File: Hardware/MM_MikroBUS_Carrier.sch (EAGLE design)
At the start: 50 parts, among them J15 MICROMOD-2222-C, J2 QWIIC_RIGHT_ANGLE, J5 Vertical Qwiic Connector, J7 MIKROBUS_SMD_BLACK1, U1 MCP73831, U2 AP7361C-33FGEUDFN-8

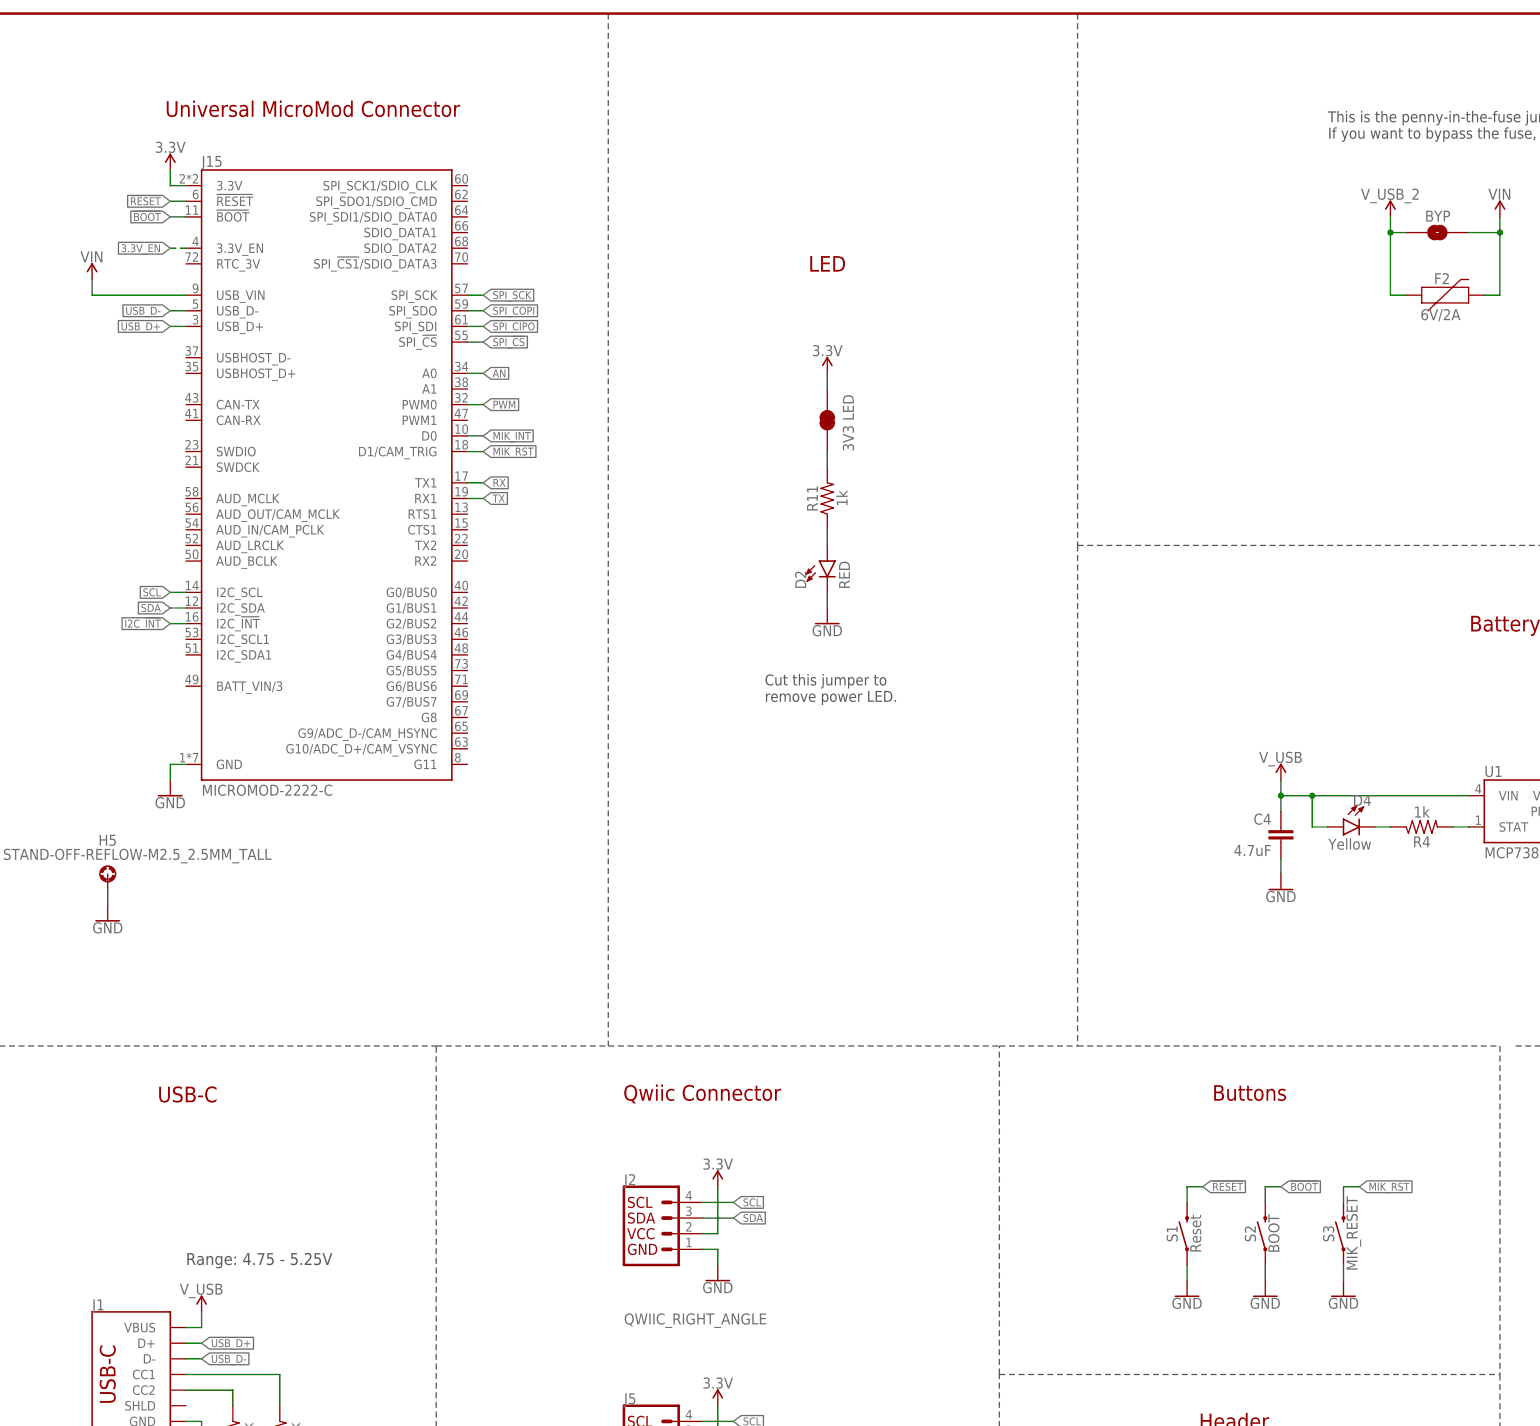
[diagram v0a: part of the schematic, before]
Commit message: MikroE updates
* Add JTAG connector
* Remove mikroE reset button
* Moved mikroBUS labels so that they can all be seen when socket is populated
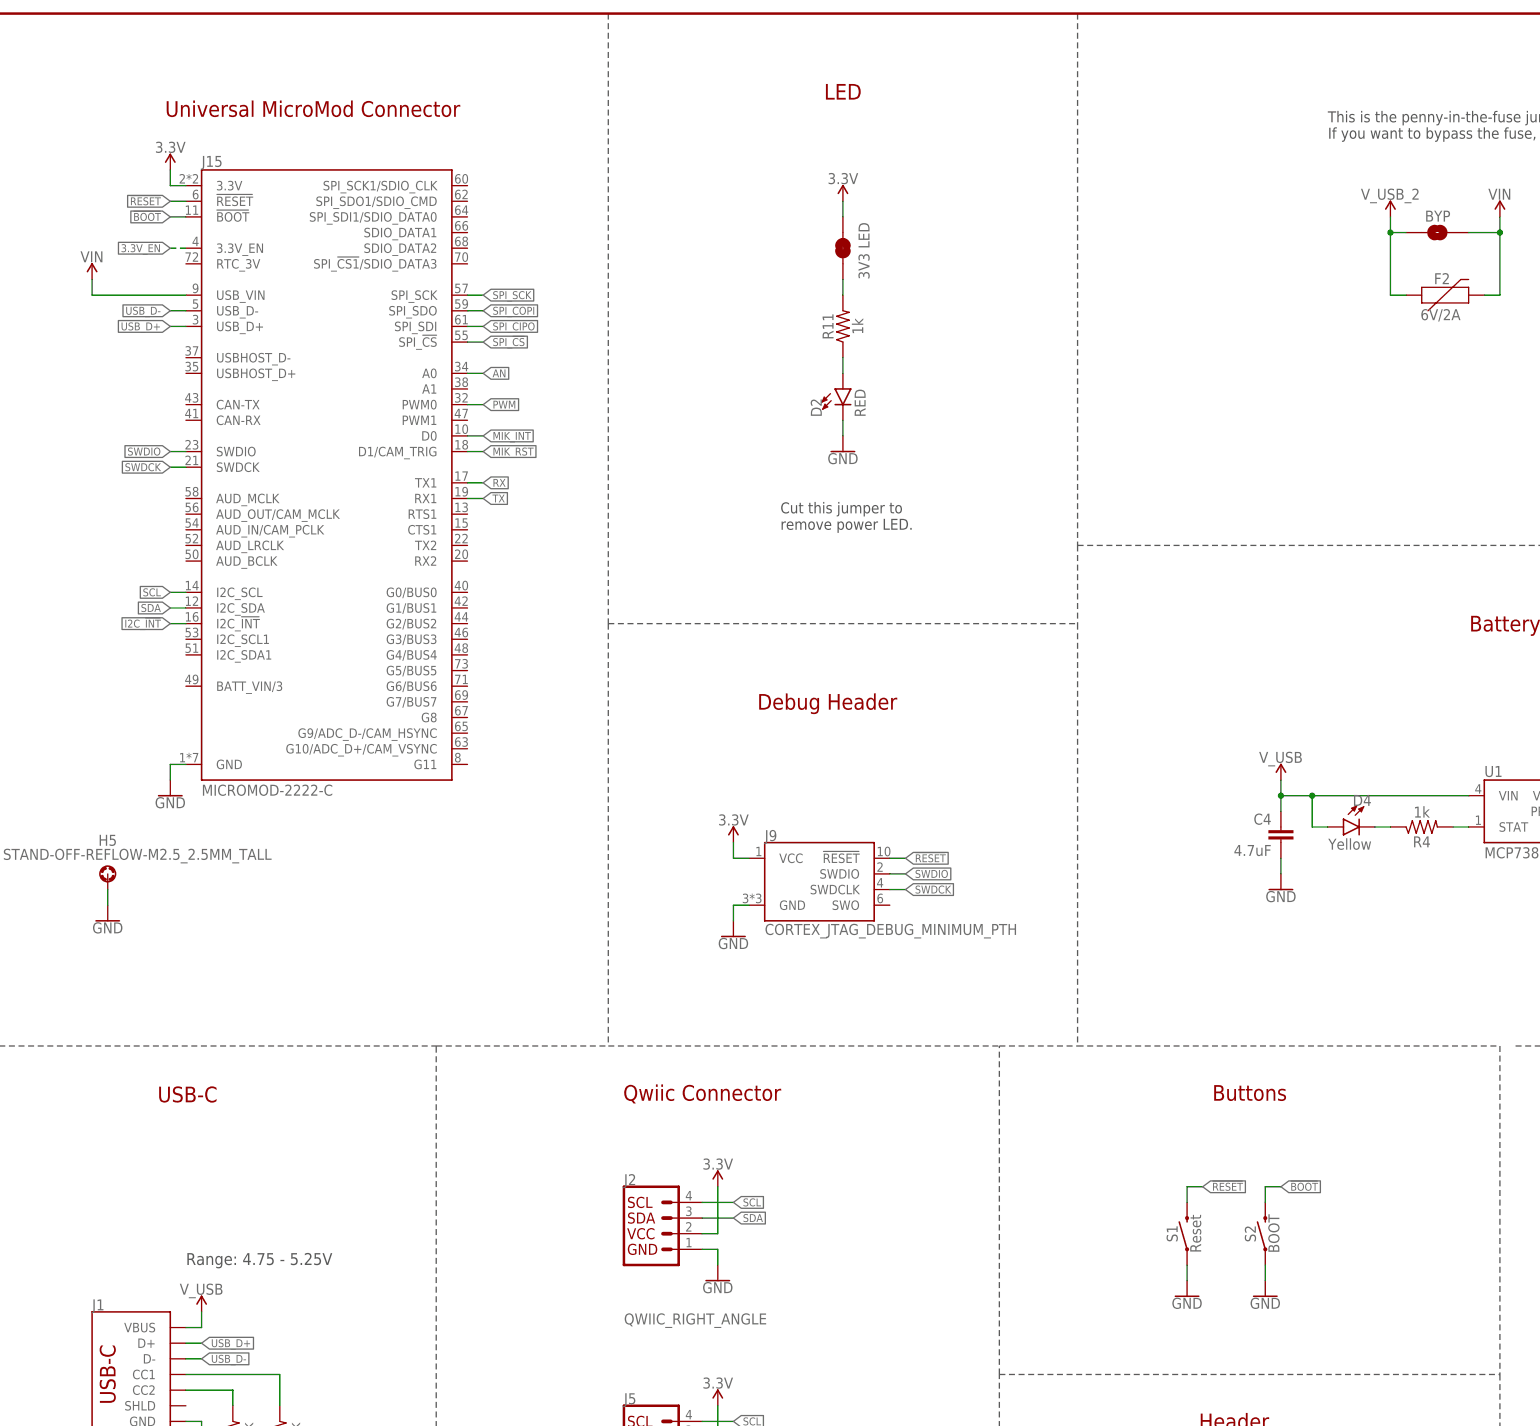
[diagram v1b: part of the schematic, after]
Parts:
- removed S3: MIK_RESET, SparkFun-Switches:MOMENTARY-SWITCH-SPST-SMD-5.2-TALL-REDUNDANT
- added J9: CORTEX_JTAG_DEBUG_MINIMUM_PTH, SparkFun-Connectors:CORTEX_JTAG_DEBUG_MINIMUM_PTH
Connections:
- new net SWDCK: J15.SWDCK, J9.SWDCLK
- new net SWDIO: J15.SWDIO, J9.SWDIO
- net !RESET!: now also J9.!RESET
- net 3.3V: now also J9.VCC
- net GND: now also J9.GND; no longer S3.1
- net MIK_RST: no longer S3.2
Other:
- note added: "Debug Header"
- moved on the sheet: D2, R11

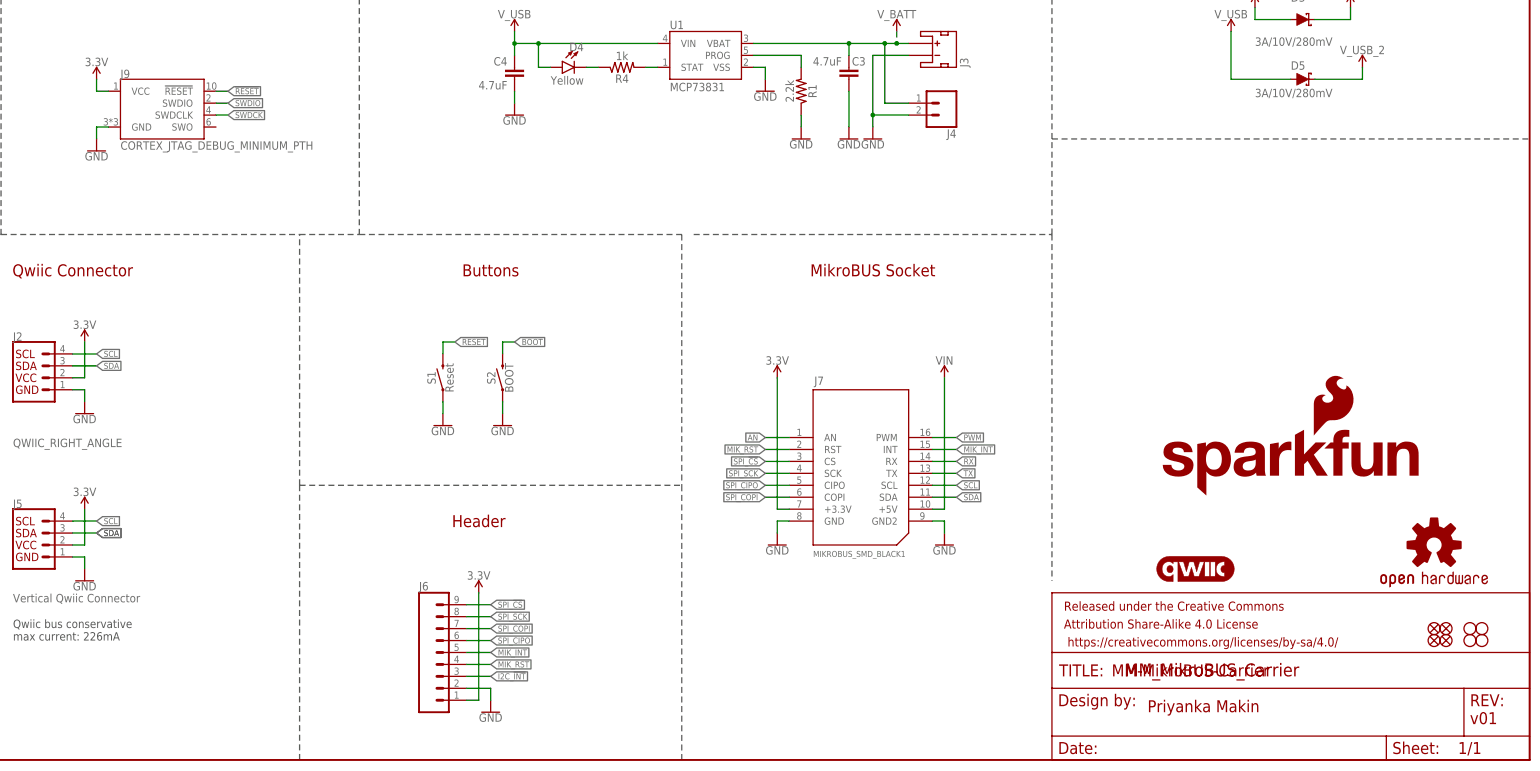
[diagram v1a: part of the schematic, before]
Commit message: Pete's updates
* Bump version number on schematic and board
* Add measures for header
* Add test points for SWDIO and SWDCK
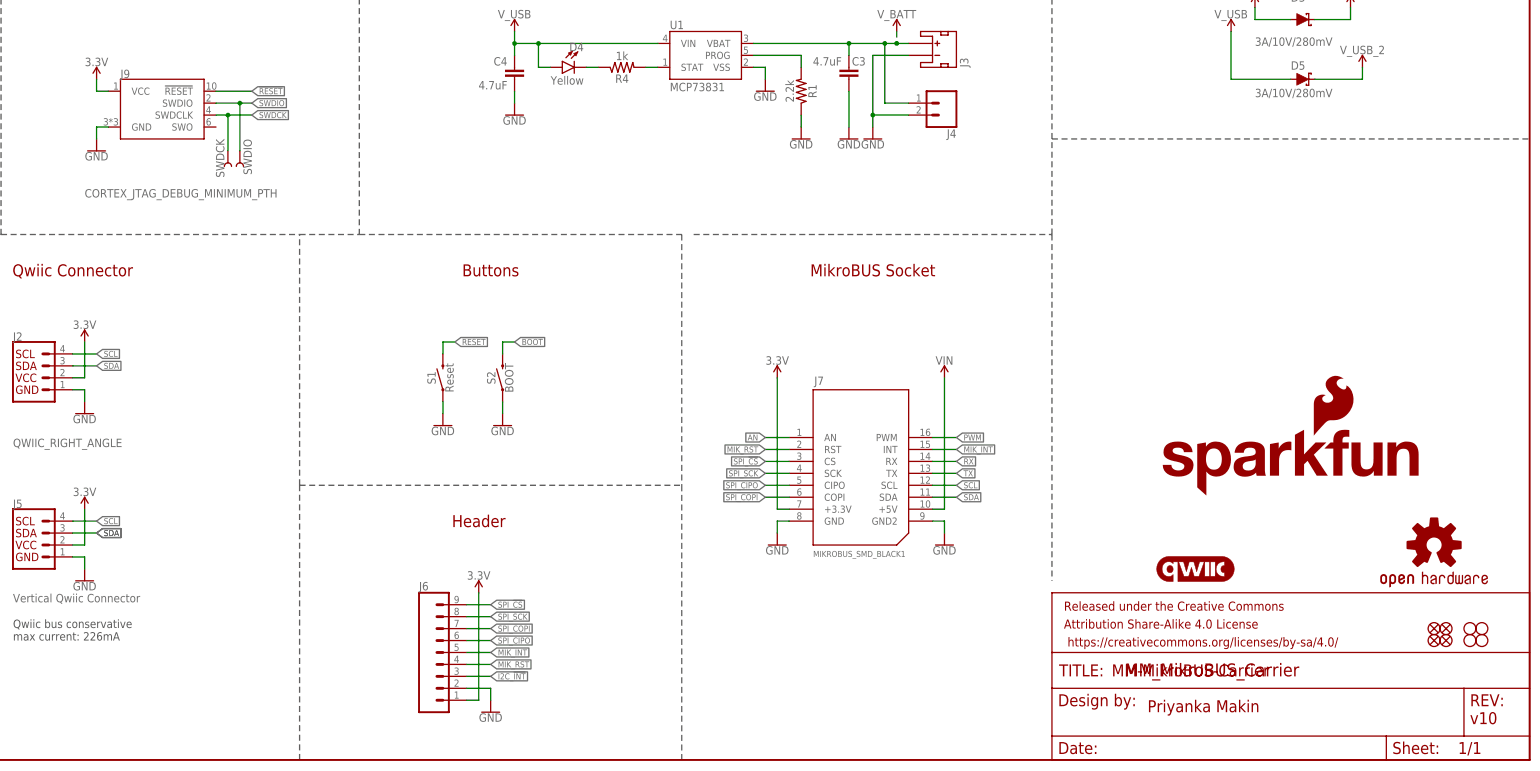
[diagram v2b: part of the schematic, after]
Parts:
- added SWDCK, SWDIO: TEST-POINT3, SparkFun-Connectors:TEST-POINT3
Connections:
- net SWDCK: now also SWDCK.1
- net SWDIO: now also SWDIO.1
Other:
- note added: "v10"
- note removed: "v01"
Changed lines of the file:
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@@
 <part name="GND13" library="SparkFun-PowerSymbols" deviceset="GND" device=""/>
 <part name="SUPPLY20" library="SparkFun-PowerSymbols" deviceset="3.3V" device=""/>
+<part name="SWDCK" library="SparkFun-Connectors" deviceset="TEST-POINT" device="3"/>
+<part name="SWDIO" library="SparkFun-Connectors" deviceset="TEST-POINT" device="3"/>
 </parts>
 <sheets>
@@
 <text x="342.9" y="17.78" size="2.54" layer="94" font="vector">MM-MikroBUS-Carrier</text>
 <text x="144.78" y="266.7" size="2.54" layer="94" font="vector" align="center">LED</text>
-<text x="419.1" y="7.62" size="2.54" layer="94" font="vector">v01</text>
+<text x="419.1" y="7.62" size="2.54" layer="94" font="vector">v10</text>
 <text x="134.62" y="195.58" size="1.778" layer="97" font="vector">Cut this jumper to
 remove power LED.</text>
@@
 <instance part="J9" gate="G$1" x="142.24" y="137.16" smashed="yes">
 <attribute name="NAME" x="132.08" y="145.034" size="1.778" layer="95" font="vector"/>
-<attribute name="VALUE" x="132.08" y="129.794" size="1.778" layer="96" font="vector"/>
+<attribute name="VALUE" x="124.46" y="119.634" size="1.778" layer="96" font="vector"/>
 </instance>
 <instance part="GND13" gate="1" x="127" y="129.54" smashed="yes">
@@
 <instance part="SUPPLY20" gate="G$1" x="127" y="144.78" smashed="yes">
 <attribute name="VALUE" x="127" y="147.574" size="1.778" layer="96" align="bottom-center"/>
+</instance>
+<instance part="SWDCK" gate="G$1" x="154.94" y="129.54" smashed="yes" rot="R270">
+<attribute name="NAME" x="152.4" y="132.08" size="1.778" layer="95" font="vector" rot="R270"/>
+</instance>
+<instance part="SWDIO" gate="G$1" x="157.48" y="129.54" smashed="yes" rot="R270">
+<attribute name="NAME" x="158.242" y="132.08" size="1.778" layer="95" font="vector" rot="R270"/>
 </instance>
 </instances>
@@
 <segment>
 <pinref part="J9" gate="G$1" pin="!RESET"/>
-<wire x1="152.4" y1="142.24" x2="154.94" y2="142.24" width="0.1524" layer="91"/>
-<label x="154.94" y="142.24" size="1.27" layer="95" xref="yes"/>
+<wire x1="152.4" y1="142.24" x2="160.02" y2="142.24" width="0.1524" layer="91"/>
+<label x="160.02" y="142.24" size="1.27" layer="95" xref="yes"/>
 </segment>
 </net>
@@
 <segment>
 <pinref part="J9" gate="G$1" pin="SWDIO"/>
-<wire x1="152.4" y1="139.7" x2="154.94" y2="139.7" width="0.1524" layer="91"/>
-<label x="154.94" y="139.7" size="1.27" layer="95" xref="yes"/>
+<wire x1="152.4" y1="139.7" x2="157.48" y2="139.7" width="0.1524" layer="91"/>
+<label x="160.02" y="139.7" size="1.27" layer="95" xref="yes"/>
+<pinref part="SWDIO" gate="G$1" pin="1"/>
+<wire x1="157.48" y1="139.7" x2="160.02" y2="139.7" width="0.1524" layer="91"/>
+<wire x1="157.48" y1="129.54" x2="157.48" y2="139.7" width="0.1524" layer="91"/>
+<junction x="157.48" y="139.7"/>
 </segment>
 <segment>
@@
 <pinref part="J9" gate="G$1" pin="SWDCLK"/>
 <wire x1="152.4" y1="137.16" x2="154.94" y2="137.16" width="0.1524" layer="91"/>
-<label x="154.94" y="137.16" size="1.27" layer="95" xref="yes"/>
-</segment>
-<segment>
+<label x="160.02" y="137.16" size="1.27" layer="95" xref="yes"/>
+<pinref part="SWDCK" gate="G$1" pin="1"/>
+<wire x1="154.94" y1="137.16" x2="160.02" y2="137.16" width="0.1524" layer="91"/>
+<wire x1="154.94" y1="129.54" x2="154.94" y2="137.16" width="0.1524" layer="91"/>
+<junction x="154.94" y="137.16"/>
+</segment>
+<segment>
